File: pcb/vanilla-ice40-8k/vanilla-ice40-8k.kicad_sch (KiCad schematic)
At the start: 12 parts, among them X1 SG-8101CE 100Mhz

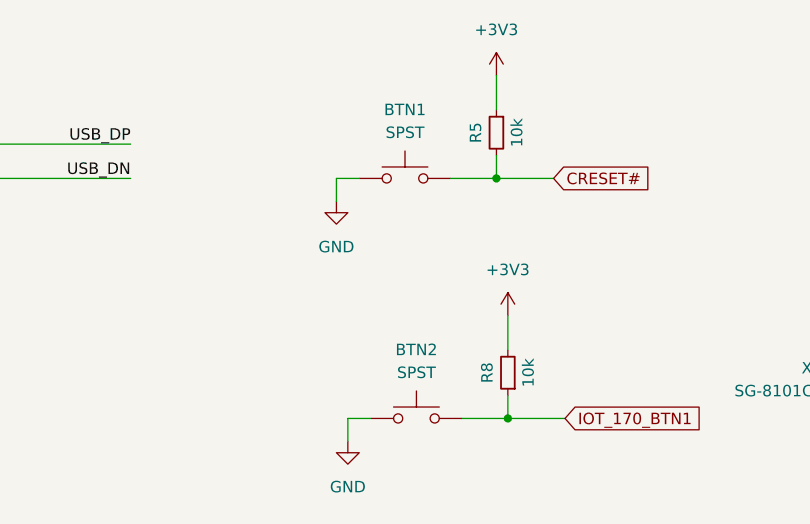
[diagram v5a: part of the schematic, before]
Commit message: [hx8k][pcb] finalize silks
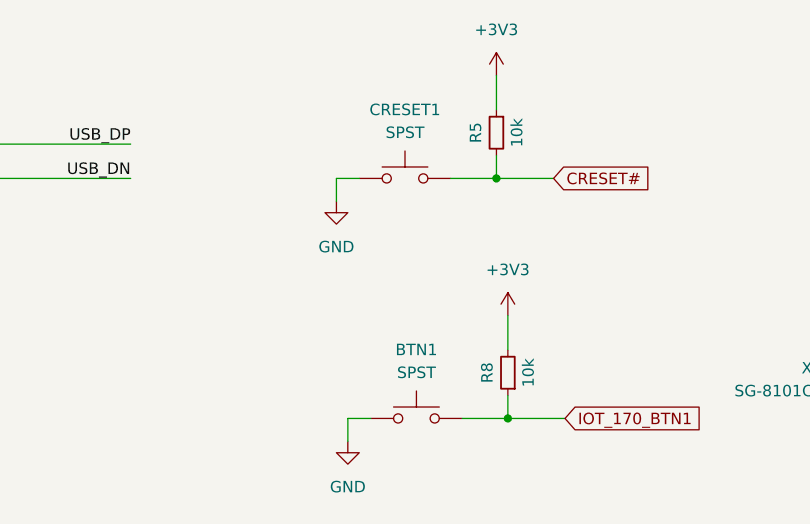
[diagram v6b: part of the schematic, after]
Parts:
- CDONE1: footprint Diode_SMD:D_0603_1608Metric -> !Misc:D_0603_1608Metric
- LED1: footprint Diode_SMD:D_0603_1608Metric -> !Misc:D_0603_1608Metric; LCSC Part # C965807 -> C434421
- PWR1: footprint Diode_SMD:D_0603_1608Metric -> !Misc:D_0603_1608Metric; LCSC Part # C2286 -> C434419
- renumbered BTN2 to BTN1, BTN1 to CRESET1
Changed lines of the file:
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@@
 			)
 		)
-		(property "Footprint" "Diode_SMD:D_0603_1608Metric"
+		(property "Footprint" "!Misc:D_0603_1608Metric"
 			(at 350.52 43.18 90)
 			(effects
@@
 			)
 		)
-		(property "Description" "Light emitting diode, small symbol"
+		(property "Description" "LED, Blue, 0603"
 			(at 350.52 43.18 0)
 			(effects
@@
 			)
 		)
-		(property "LCSC Part #" "C965807"
+		(property "LCSC Part #" "C434421"
 			(at 350.52 43.18 0)
 			(effects
@@
 		(dnp no)
 		(fields_autoplaced yes)
-		(property "Reference" "BTN2"
+		(property "Reference" "BTN1"
 			(at 186.69 52.07 0)
 			(effects
@@
 			(project "vanilla-ice40-8k"
 				(path "/6fdfbf4b-014a-4077-8dc3-7ce5ecaf5fe5"
-					(reference "BTN2")
+					(reference "BTN1")
 					(unit 1)
 				)
@@
 			)
 		)
-		(property "Footprint" "Diode_SMD:D_0603_1608Metric"
+		(property "Footprint" "!Misc:D_0603_1608Metric"
 			(at 299.72 43.18 90)
 			(effects
@@
 			)
 		)
-		(property "Description" "Light emitting diode, small symbol"
+		(property "Description" "LED, Green, 0603"
 			(at 299.72 43.18 0)
 			(effects
@@
 			)
 		)
-		(property "Footprint" "Diode_SMD:D_0603_1608Metric"
+		(property "Footprint" "!Misc:D_0603_1608Metric"
 			(at 323.85 43.18 90)
 			(effects
@@
 			)
 		)
-		(property "Description" "Light emitting diode, small symbol"
+		(property "Description" "LED, Red, 0603"
 			(at 323.85 43.18 0)
 			(effects
@@
 			)
 		)
-		(property "LCSC Part #" "C2286"
+		(property "LCSC Part #" "C434419"
 			(at 323.85 43.18 0)
 			(effects
@@
 		(dnp no)
 		(fields_autoplaced yes)
-		(property "Reference" "BTN1"
+		(property "Reference" "CRESET1"
 			(at 185.42 25.4 0)
 			(effects
@@
 			(project "vanilla-ice40-8k"
 				(path "/6fdfbf4b-014a-4077-8dc3-7ce5ecaf5fe5"
-					(reference "BTN1")
-					(unit 1)
-				)
+					(reference "CRESET1")
+					(unit 1)
+				)

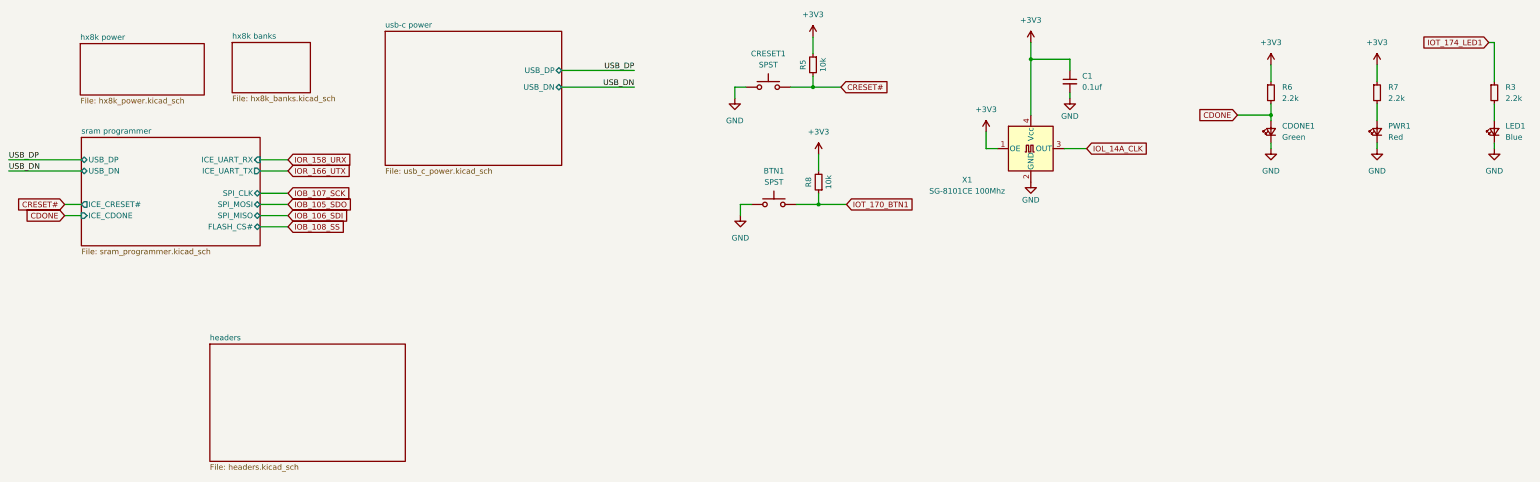
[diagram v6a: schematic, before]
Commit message: [hx8k][pcb] convert all components to custom lib
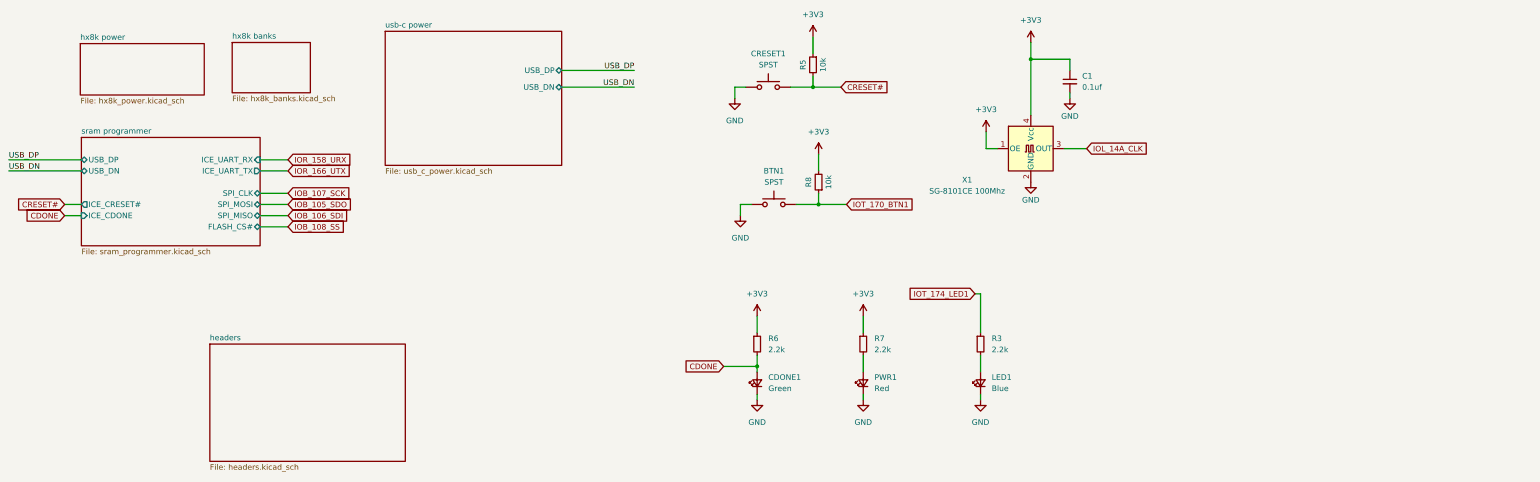
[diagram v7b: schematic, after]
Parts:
- R3, R6, R7: LCSC Part # C4190 -> C25879
- X1: footprint Oscillator:Oscillator_SMD_SeikoEpson_SG8002CE-4Pin_3.2x2.5mm -> !Misc:Oscillator_SMD_SeikoEpson_SG8002CE-4Pin_3.2x2.5mm
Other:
- moved on the sheet: CDONE1, LED1, PWR1, R3, R6, R7

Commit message: [pcb] misc fixes during jlcpcb production submission
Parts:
- R3, R6, R7: LCSC Part # C25879 -> C4190
